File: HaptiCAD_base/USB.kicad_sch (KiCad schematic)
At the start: 5 parts, among them J301 USB_C_Receptacle_USB2.0_16P

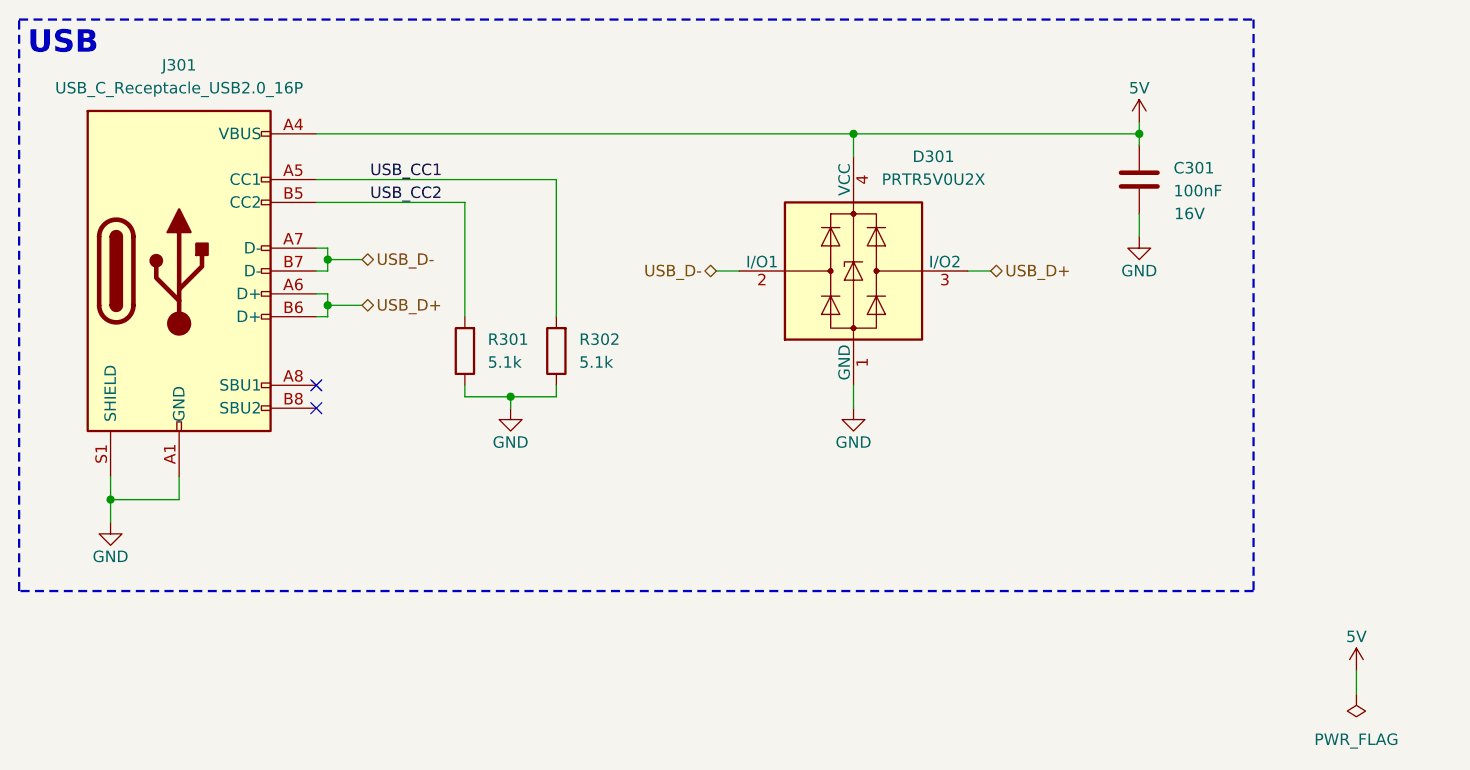
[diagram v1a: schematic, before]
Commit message: Finished schematic of the base board
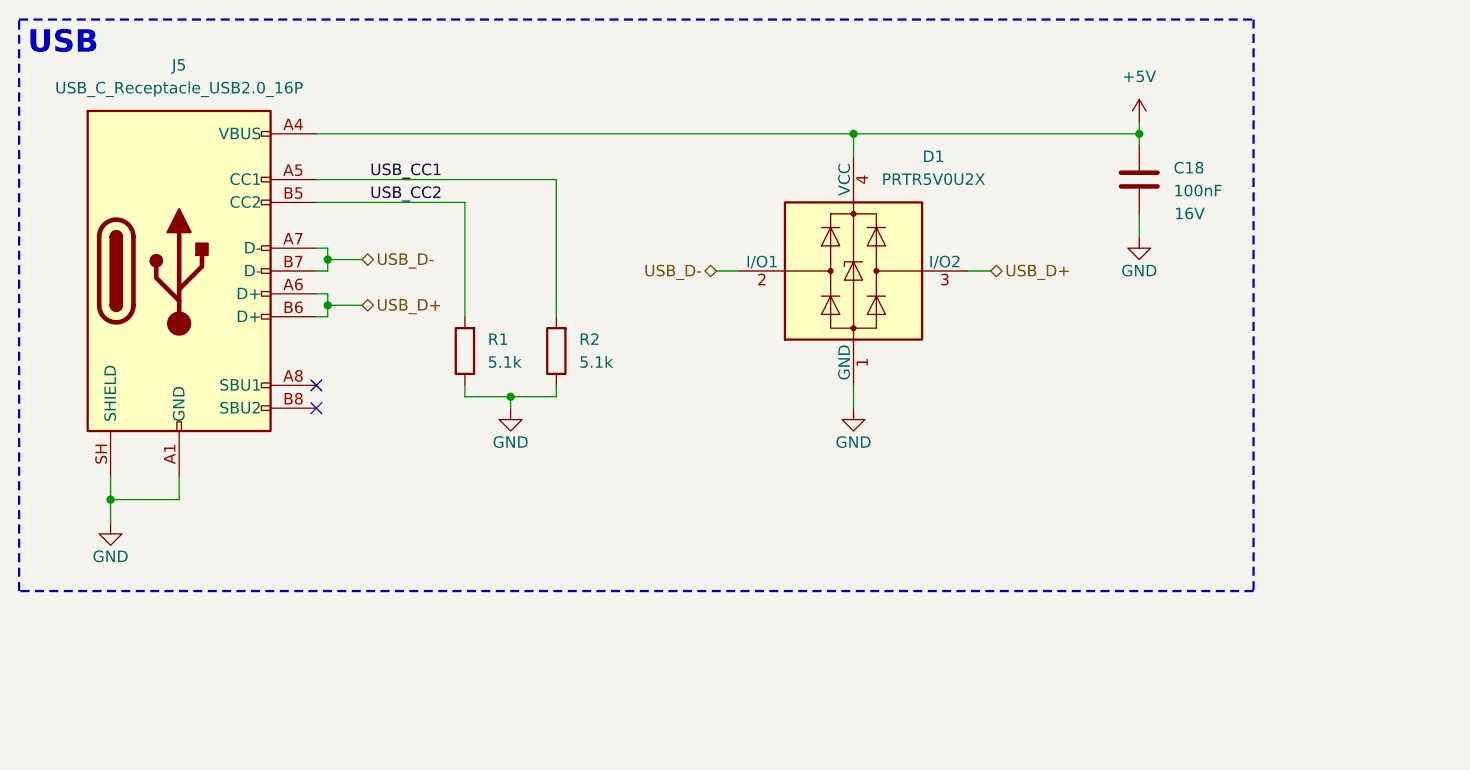
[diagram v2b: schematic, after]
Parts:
- renumbered C301 to C18, D301 to D1, J301 to J5, R301 to R1, R302 to R2
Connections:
- net GND: now also J5.SH (SHIELD); no longer J5.S1 (SHIELD)
- net 5V renamed +5V
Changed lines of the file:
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@@
-	(wire
-		(pts
-			(xy 186.69 110.49) (xy 186.69 113.03)
-		)
-		(stroke
-			(width 0)
-			(type default)
-		)
-	)
 	(wire
 		(pts
@@
 		(dnp no)
 		(fields_autoplaced yes)
-		(property "Reference" "J301"
+		(property "Reference" "J5"
 			(at 55.88 43.18 0)
 			(show_name no)
@@
 		(pin "B9"
 		)
-		(pin "S1"
+		(pin "SH"
 		)
 		(pin "A12"
@@
 			(project "HaptiCAD_base"
 				(path "/09c102b8-dfc1-4666-b1e2-d0c53b401993/e939acba-a336-4e5f-bfb8-79d3cd46c7a7"
-					(reference "J301")
+					(reference "J5")
 					(unit 1)
 				)
@@
 		(in_pos_files yes)
 		(dnp no)
-		(property "Reference" "D301"
+		(property "Reference" "D1"
 			(at 139.7 53.34 0)
 			(show_name no)
@@
 			(project "HaptiCAD_base"
 				(path "/09c102b8-dfc1-4666-b1e2-d0c53b401993/e939acba-a336-4e5f-bfb8-79d3cd46c7a7"
-					(reference "D301")
+					(reference "D1")
 					(unit 1)
 				)
@@
 	)
 	(symbol
-		(lib_id "PCM_SparkFun-PowerSymbol:GND")
+		(lib_id "power:GND")
 		(at 92.71 81.28 0)
 		(unit 1)
@@
 		(dnp no)
 		(fields_autoplaced yes)
-		(property "Reference" "#PWR0302"
+		(property "Reference" "#PWR061"
 			(at 92.71 87.63 0)
 			(hide yes)
@@
 		)
 		(property "Description" "Power symbol creates a global label with name \"GND\" , ground"
-			(at 92.71 90.17 0)
+			(at 92.71 81.28 0)
 			(hide yes)
 			(show_name no)
@@
 			(project "HaptiCAD_base"
 				(path "/09c102b8-dfc1-4666-b1e2-d0c53b401993/e939acba-a336-4e5f-bfb8-79d3cd46c7a7"
-					(reference "#PWR0302")
+					(reference "#PWR061")
 					(unit 1)
 				)
@@
 	)
 	(symbol
-		(lib_id "PCM_SparkFun-PowerSymbol:GND")
+		(lib_id "power:GND")
 		(at 130.81 81.28 0)
 		(unit 1)
@@
 		(dnp no)
 		(fields_autoplaced yes)
-		(property "Reference" "#PWR0303"
+		(property "Reference" "#PWR062"
 			(at 130.81 87.63 0)
 			(hide yes)
@@
 		)
 		(property "Description" "Power symbol creates a global label with name \"GND\" , ground"
-			(at 130.81 90.17 0)
+			(at 130.81 81.28 0)
 			(hide yes)
 			(show_name no)
@@
 			(project "HaptiCAD_base"
 				(path "/09c102b8-dfc1-4666-b1e2-d0c53b401993/e939acba-a336-4e5f-bfb8-79d3cd46c7a7"
-					(reference "#PWR0303")
+					(reference "#PWR062")
 					(unit 1)
 				)
@@
 	)
 	(symbol
-		(lib_id "PCM_SparkFun-PowerSymbol:GND")
+		(lib_id "power:GND")
 		(at 48.26 93.98 0)
 		(unit 1)
@@
 		(dnp no)
 		(fields_autoplaced yes)
-		(property "Reference" "#PWR0301"
+		(property "Reference" "#PWR060"
 			(at 48.26 100.33 0)
 			(hide yes)
@@
 		)
 		(property "Description" "Power symbol creates a global label with name \"GND\" , ground"
-			(at 48.26 102.87 0)
+			(at 48.26 93.98 0)
 			(hide yes)
 			(show_name no)
@@
 			(project "HaptiCAD_base"
 				(path "/09c102b8-dfc1-4666-b1e2-d0c53b401993/e939acba-a336-4e5f-bfb8-79d3cd46c7a7"
-					(reference "#PWR0301")
+					(reference "#PWR060")
 					(unit 1)
 				)
@@
 		(dnp no)
 		(fields_autoplaced yes)
-		(property "Reference" "R302"
+		(property "Reference" "R2"
 			(at 100.33 73.6599 0)
 			(show_name no)
@@
 			(project "HaptiCAD_base"
 				(path "/09c102b8-dfc1-4666-b1e2-d0c53b401993/e939acba-a336-4e5f-bfb8-79d3cd46c7a7"
-					(reference "R302")
+					(reference "R2")
 					(unit 1)
 				)
@@
 	)
 	(symbol
-		(lib_id "PCM_SparkFun-PowerSymbol:5V")
+		(lib_id "power:+5V")
 		(at 162.56 49.53 0)
 		(unit 1)
@@
 		(dnp no)
 		(fields_autoplaced yes)
-		(property "Reference" "#PWR0304"
+		(property "Reference" "#PWR063"
 			(at 162.56 53.34 0)
 			(hide yes)
@@
 			)
 		)
-		(property "Value" "5V"
-			(at 162.56 45.72 0)
-			(show_name no)
-			(do_not_autoplace yes)
+		(property "Value" "+5V"
+			(at 162.56 44.45 0)
+			(show_name no)
+			(do_not_autoplace no)
 			(effects
 				(font
@@
 			)
 		)
-		(property "Description" "Power symbol creates a global label with name \"5V\""
-			(at 162.56 55.88 0)
+		(property "Description" "Power symbol creates a global label with name \"+5V\""
+			(at 162.56 49.53 0)
 			(hide yes)
 			(show_name no)
@@
 			(project "HaptiCAD_base"
 				(path "/09c102b8-dfc1-4666-b1e2-d0c53b401993/e939acba-a336-4e5f-bfb8-79d3cd46c7a7"
-					(reference "#PWR0304")
+					(reference "#PWR063")
 					(unit 1)
 				)
@@
 	)
 	(symbol
-		(lib_id "PCM_SparkFun-PowerSymbol:GND")
+		(lib_id "power:GND")
 		(at 162.56 62.23 0)
 		(unit 1)
@@
 		(dnp no)
 		(fields_autoplaced yes)
-		(property "Reference" "#PWR0305"
+		(property "Reference" "#PWR064"
 			(at 162.56 68.58 0)
 			(hide yes)
@@
 		)
 		(property "Description" "Power symbol creates a global label with name \"GND\" , ground"
-			(at 162.56 71.12 0)
+			(at 162.56 62.23 0)
 			(hide yes)
 			(show_name no)
@@
 			(project "HaptiCAD_base"
 				(path "/09c102b8-dfc1-4666-b1e2-d0c53b401993/e939acba-a336-4e5f-bfb8-79d3cd46c7a7"
-					(reference "#PWR0305")
-					(unit 1)
-				)
-			)
-		)
-	)
-	(symbol
-		(lib_id "power:PWR_FLAG")
-		(at 186.69 113.03 180)
-		(unit 1)
-		(body_style 1)
-		(exclude_from_sim no)
-		(in_bom yes)
-		(on_board yes)
-		(in_pos_files yes)
-		(dnp no)
-		(fields_autoplaced yes)
-		(property "Reference" "#FLG0301"
-			(at 186.69 114.935 0)
-			(hide yes)
-			(show_name no)
-			(do_not_autoplace no)
-			(effects
-				(font
-					(size 1.27 1.27)
-				)
-			)
-		)
-		(property "Value" "PWR_FLAG"
-			(at 186.69 118.11 0)
-			(show_name no)
-			(do_not_autoplace no)
-			(effects
-				(font
-					(size 1.27 1.27)
-				)
-			)
-		)
-		(property "Footprint" ""
-			(at 186.69 113.03 0)
-			(hide yes)
-			(show_name no)
-			(do_not_autoplace no)
-			(effects
-				(font
-					(size 1.27 1.27)
-				)
-			)
-		)
-		(property "Datasheet" ""
-			(at 186.69 113.03 0)
-			(hide yes)
-			(show_name no)
-			(do_not_autoplace no)
-			(effects
-				(font
-					(size 1.27 1.27)
-				)
-			)
-		)
-		(property "Description" "Special symbol for telling ERC where power comes from"
-			(at 186.69 113.03 0)
-			(hide yes)
-			(show_name no)
-			(do_not_autoplace no)
-			(effects
-				(font
-					(size 1.27 1.27)
-				)
-			)
-		)
-		(pin "1"
-		)
-		(instances
-			(project "HaptiCAD_base"
-				(path "/09c102b8-dfc1-4666-b1e2-d0c53b401993/e939acba-a336-4e5f-bfb8-79d3cd46c7a7"
-					(reference "#FLG0301")
+					(reference "#PWR064")
 					(unit 1)
 				)
@@
 		(dnp no)
 		(fields_autoplaced yes)
-		(property "Reference" "R301"
+		(property "Reference" "R1"
 			(at 90.17 73.6599 0)
 			(show_name no)
@@
 			(project "HaptiCAD_base"
 				(path "/09c102b8-dfc1-4666-b1e2-d0c53b401993/e939acba-a336-4e5f-bfb8-79d3cd46c7a7"
-					(reference "R301")
+					(reference "R1")
 					(unit 1)
 				)
@@
 		(in_pos_files yes)
 		(dnp no)
-		(property "Reference" "C301"
+		(property "Reference" "C18"
 			(at 166.37 54.6099 0)
 			(show_name no)
@@
 			(project "HaptiCAD_base"
 				(path "/09c102b8-dfc1-4666-b1e2-d0c53b401993/e939acba-a336-4e5f-bfb8-79d3cd46c7a7"
-					(reference "C301")
+					(reference "C18")
 					(unit 1)
 				)
-			)
-		)
-	)
-	(symbol
-		(lib_id "PCM_SparkFun-PowerSymbol:5V")
-		(at 186.69 110.49 0)
-		(unit 1)
-		(body_style 1)
-		(exclude_from_sim no)
-		(in_bom yes)
-		(on_board yes)
-		(in_pos_files yes)
-		(dnp no)
-		(property "Reference" "#PWR0306"
-			(at 186.69 114.3 0)
-			(hide yes)
-			(show_name no)
-			(do_not_autoplace no)
-			(effects
-				(font
-					(size 1.27 1.27)
-				)
-			)
-		)
-		(property "Value" "5V"
-			(at 186.69 106.68 0)
-			(show_name no)
-			(do_not_autoplace yes)
-			(effects
-				(font
-					(size 1.27 1.27)
-				)
-			)
-		)
-		(property "Footprint" ""
-			(at 186.69 110.49 0)
-			(hide yes)
-			(show_name no)
-			(do_not_autoplace no)
-			(effects
-				(font
-					(size 1.27 1.27)
-				)
-			)
-		)
-		(property "Datasheet" ""
-			(at 186.69 110.49 0)
-			(hide yes)
-			(show_name no)
-			(do_not_autoplace no)
-			(effects
-				(font
-					(size 1.27 1.27)
-				)
-			)
-		)
-		(property "Description" "Power symbol creates a global label with name \"5V\""
-			(at 186.69 116.84 0)
-			(hide yes)
-			(show_name no)
-			(do_not_autoplace no)
-			(effects
-				(font
-					(size 1.27 1.27)
-				)
-			)
-		)
-		(pin "1"
-		)
-		(instances
-			(project "HaptiCAD_base"
-				(path "/09c102b8-dfc1-4666-b1e2-d0c53b401993/e939acba-a336-4e5f-bfb8-79d3cd46c7a7"
-					(reference "#PWR0306")
-					(unit 1)
-				)

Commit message: Finished the layout for the base and motor mount
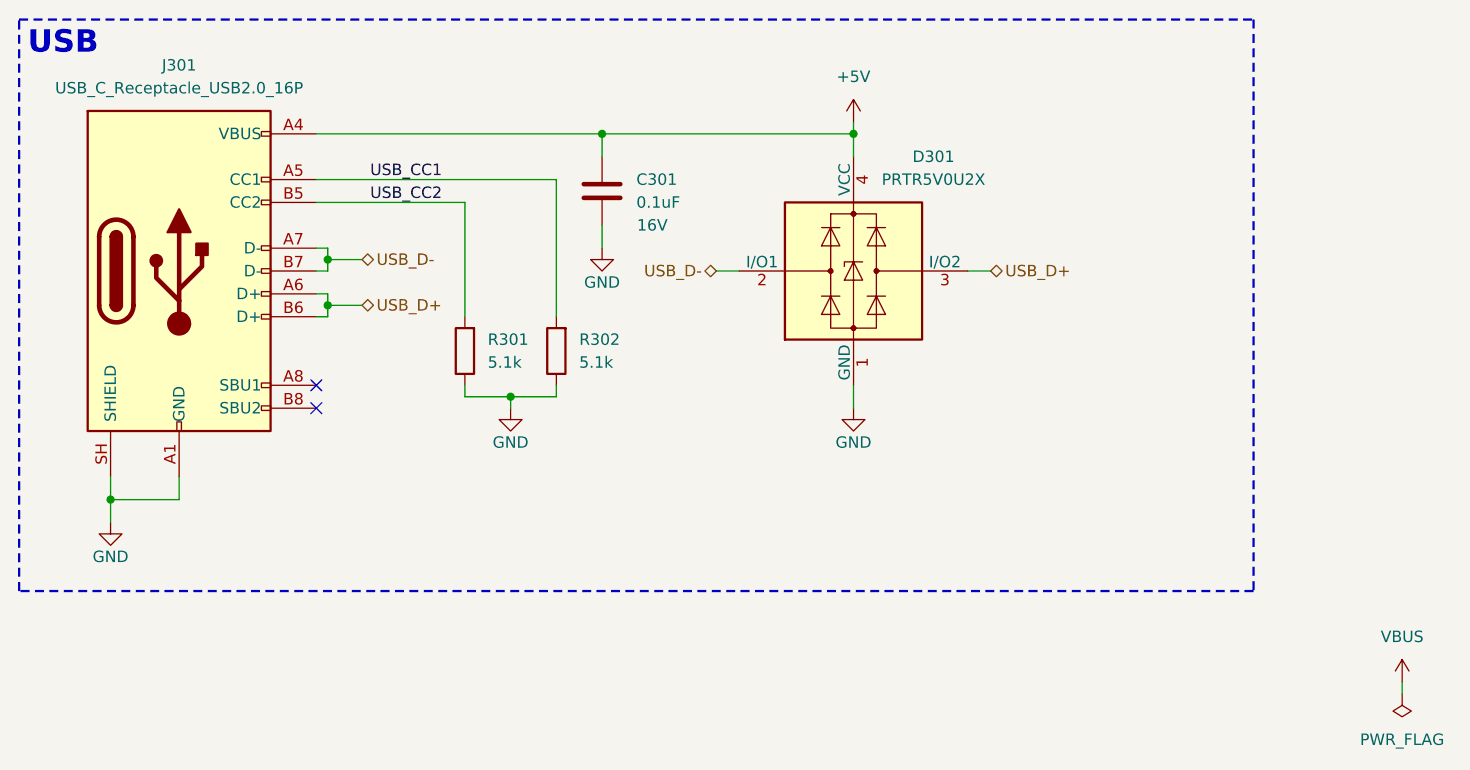
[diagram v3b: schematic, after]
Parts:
- C301: renamed from C18; value 100nF -> 0.1uF
- J301: renamed from J5; footprint Connector_USB:USB_C_Receptacle_G-Switch_GT-USB-7010ASV -> PCM_marbastlib-various:USB_C_Receptacle_HRO_TYPE-C-31-M-14
- renumbered D1 to D301, R1 to R301, R2 to R302
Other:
- moved on the sheet: C301
